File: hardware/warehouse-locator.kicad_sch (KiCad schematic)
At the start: 12 parts, among them J1 Screw_Terminal_01x03, J2 Screw_Terminal_01x03, J3 Screw_Terminal_01x03, J4 Barrel_Jack, J5 Screw_Terminal_01x03, J6 Screw_Terminal_01x03, J7 Screw_Terminal_01x03, J8 Ethernet, U1 ESP32-DevKitC

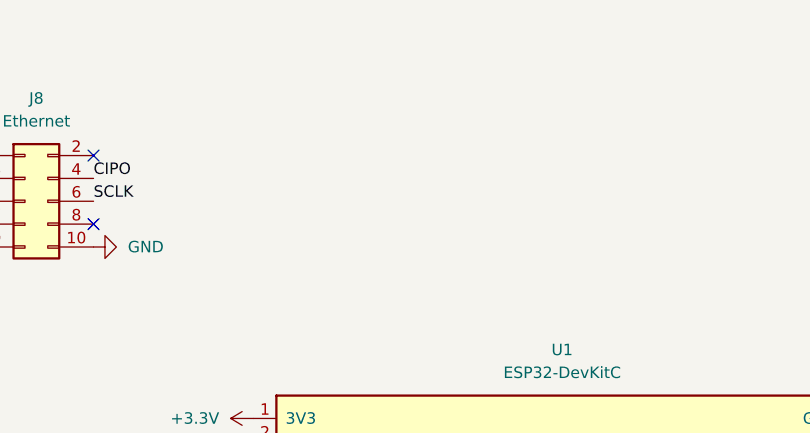
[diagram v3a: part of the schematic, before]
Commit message: Add Status LED
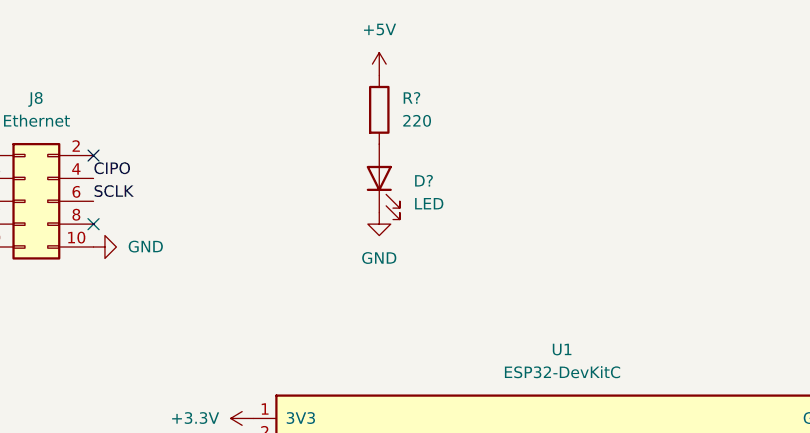
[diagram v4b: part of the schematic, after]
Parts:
- added D?: LED, LED_THT:LED_D5.0mm, symbol Device:LED
- added R?: 220, Resistor_THT:R_Axial_DIN0207_L6.3mm_D2.5mm_P10.16mm_Horizontal, symbol Device:R
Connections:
- net +5V: now also R?.1
- net GND: now also D?.1 (K)
- new net: D?.2 (A), R?.2
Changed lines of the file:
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@@
     (pin "3")
+  )
+  (symbol (lib_id "Device:LED") (at 179.07 54.61 90) (unit 1)
+    (in_bom yes) (on_board yes) (fields_autoplaced)
+    (property "Reference" "D?" (id 0) (at 182.88 54.9274 90)
+      (effects (font (size 1.27 1.27)) (justify right))
+    )
+    (property "Value" "LED" (id 1) (at 182.88 57.4674 90)
+      (effects (font (size 1.27 1.27)) (justify right))
+    )
+    (property "Footprint" "LED_THT:LED_D5.0mm" (id 2) (at 179.07 54.61 0)
+      (effects (font (size 1.27 1.27)) hide)
+    )
+    (property "Datasheet" "~" (id 3) (at 179.07 54.61 0)
+      (effects (font (size 1.27 1.27)) hide)
+    )
+    (pin "1")
+    (pin "2")
   )
   (symbol (lib_name "GND_1") (lib_id "power:GND") (at 238.76 81.28 90) (unit 1)
@@
       (effects (font (size 1.27 1.27)) hide)
     )
+  )
+  (symbol (lib_name "GND_3") (lib_id "power:GND") (at 179.07 58.42 0) (unit 1)
+    (in_bom yes) (on_board yes) (fields_autoplaced)
+    (property "Reference" "#PWR?" (id 0) (at 179.07 64.77 0)
+      (effects (font (size 1.27 1.27)) hide)
+    )
+    (property "Value" "GND" (id 1) (at 179.07 63.5 0))
+    (property "Footprint" "" (id 2) (at 179.07 58.42 0)
+      (effects (font (size 1.27 1.27)) hide)
+    )
+    (property "Datasheet" "" (id 3) (at 179.07 58.42 0)
+      (effects (font (size 1.27 1.27)) hide)
+    )
+    (pin "1")
   )
   (symbol (lib_id "power:+5V") (at 59.69 101.6 0) (unit 1)
@@
     (pin "1")
   )
+  (symbol (lib_name "+5V_1") (lib_id "power:+5V") (at 179.07 43.18 0) (unit 1)
+    (in_bom yes) (on_board yes) (fields_autoplaced)
+    (property "Reference" "#PWR?" (id 0) (at 179.07 46.99 0)
+      (effects (font (size 1.27 1.27)) hide)
+    )
+    (property "Value" "+5V" (id 1) (at 179.07 38.1 0))
+    (property "Footprint" "" (id 2) (at 179.07 43.18 0)
+      (effects (font (size 1.27 1.27)) hide)
+    )
+    (property "Datasheet" "" (id 3) (at 179.07 43.18 0)
+      (effects (font (size 1.27 1.27)) hide)
+    )
+    (pin "1")
+  )
   (symbol (lib_id "Connector:Screw_Terminal_01x03") (at 102.87 105.41 0) (unit 1)
     (in_bom yes) (on_board yes) (fields_autoplaced)
@@
     (pin "2")
     (pin "3")
+  )
+  (symbol (lib_id "Device:R") (at 179.07 46.99 0) (unit 1)
+    (in_bom yes) (on_board yes) (fields_autoplaced)
+    (property "Reference" "R?" (id 0) (at 181.61 45.7199 0)
+      (effects (font (size 1.27 1.27)) (justify left))
+    )
+    (property "Value" "220" (id 1) (at 181.61 48.2599 0)
+      (effects (font (size 1.27 1.27)) (justify left))
+    )
+    (property "Footprint" "Resistor_THT:R_Axial_DIN0207_L6.3mm_D2.5mm_P10.16mm_Horizontal" (id 2) (at 177.292 46.99 90)
+      (effects (font (size 1.27 1.27)) hide)
+    )
+    (property "Datasheet" "~" (id 3) (at 179.07 46.99 0)
+      (effects (font (size 1.27 1.27)) hide)
+    )
+    (pin "1")
+    (pin "2")
   )
   (symbol (lib_id "power:GND") (at 59.69 130.81 0) (unit 1)
@@
       (reference "#PWR?") (unit 1) (value "GND") (footprint "")
     )
+    (path "/49326297-d7a8-49d2-98aa-68a298420de1"
+      (reference "#PWR?") (unit 1) (value "GND") (footprint "")
+    )
     (path "/b6dc58df-5635-4bfb-a0b6-f31ca3e9691d"
       (reference "#PWR?") (unit 1) (value "GND") (footprint "")
@@
       (reference "#PWR?") (unit 1) (value "+3.3V") (footprint "")
     )
+    (path "/bbb94cab-5b50-47f4-b8eb-61d575e804ee"
+      (reference "#PWR?") (unit 1) (value "+5V") (footprint "")
+    )
+    (path "/1db8de92-1b7e-4ee2-8b02-085abde4cb76"
+      (reference "D?") (unit 1) (value "LED") (footprint "LED_THT:LED_D5.0mm")
+    )
     (path "/3f6f5fd4-bf84-4f5a-b527-b698f4821ee8"
       (reference "H1") (unit 1) (value "MountingHole") (footprint "MountingHole:MountingHole_3.2mm_M3_DIN965_Pad")
@@
       (reference "J8") (unit 1) (value "Ethernet") (footprint "Connector_PinSocket_2.54mm:PinSocket_2x05_P2.54mm_Vertical")
     )
+    (path "/cb16680a-c0f0-4315-a6bd-4d57dd5f9f7f"
+      (reference "R?") (unit 1) (value "220") (footprint "Resistor_THT:R_Axial_DIN0207_L6.3mm_D2.5mm_P10.16mm_Horizontal")
+    )
     (path "/8a6d48a6-b7bb-4a02-b51b-9f669ac7dca2"

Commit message: Commit missing file
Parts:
- gave numbers to parts that had none: 2
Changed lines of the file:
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@@
   (symbol (lib_id "power:+5V") (at 165.1 127 90) (unit 1)
     (in_bom yes) (on_board yes)
-    (property "Reference" "#PWR?" (id 0) (at 168.91 127 0)
+    (property "Reference" "#PWR019" (id 0) (at 168.91 127 0)
       (effects (font (size 1.27 1.27)) hide)
     )
@@
   (symbol (lib_name "GND_2") (lib_id "power:GND") (at 165.1 114.3 270) (unit 1)
     (in_bom yes) (on_board yes) (fields_autoplaced)
-    (property "Reference" "#PWR?" (id 0) (at 158.75 114.3 0)
+    (property "Reference" "#PWR018" (id 0) (at 158.75 114.3 0)
       (effects (font (size 1.27 1.27)) hide)
     )
@@
   (symbol (lib_id "Device:LED") (at 179.07 54.61 90) (unit 1)
     (in_bom yes) (on_board yes) (fields_autoplaced)
-    (property "Reference" "D?" (id 0) (at 182.88 54.9274 90)
+    (property "Reference" "D1" (id 0) (at 182.88 54.9274 90)
       (effects (font (size 1.27 1.27)) (justify right))
     )
@@
   (symbol (lib_name "GND_1") (lib_id "power:GND") (at 238.76 81.28 90) (unit 1)
     (in_bom yes) (on_board yes) (fields_autoplaced)
-    (property "Reference" "#PWR?" (id 0) (at 245.11 81.28 0)
+    (property "Reference" "#PWR022" (id 0) (at 245.11 81.28 0)
       (effects (font (size 1.27 1.27)) hide)
     )
@@
   (symbol (lib_name "GND_3") (lib_id "power:GND") (at 179.07 58.42 0) (unit 1)
     (in_bom yes) (on_board yes) (fields_autoplaced)
-    (property "Reference" "#PWR?" (id 0) (at 179.07 64.77 0)
+    (property "Reference" "#PWR021" (id 0) (at 179.07 64.77 0)
       (effects (font (size 1.27 1.27)) hide)
     )
@@
   (symbol (lib_name "GND_1") (lib_id "power:GND") (at 238.76 96.52 90) (unit 1)
     (in_bom yes) (on_board yes) (fields_autoplaced)
-    (property "Reference" "#PWR?" (id 0) (at 245.11 96.52 0)
+    (property "Reference" "#PWR023" (id 0) (at 245.11 96.52 0)
       (effects (font (size 1.27 1.27)) hide)
     )
@@
   (symbol (lib_id "power:+3.3V") (at 165.1 81.28 90) (unit 1)
     (in_bom yes) (on_board yes) (fields_autoplaced)
-    (property "Reference" "#PWR?" (id 0) (at 168.91 81.28 0)
+    (property "Reference" "#PWR017" (id 0) (at 168.91 81.28 0)
       (effects (font (size 1.27 1.27)) hide)
     )
@@
   (symbol (lib_name "+5V_1") (lib_id "power:+5V") (at 179.07 43.18 0) (unit 1)
     (in_bom yes) (on_board yes) (fields_autoplaced)
-    (property "Reference" "#PWR?" (id 0) (at 179.07 46.99 0)
+    (property "Reference" "#PWR020" (id 0) (at 179.07 46.99 0)
       (effects (font (size 1.27 1.27)) hide)
     )
@@
   (symbol (lib_id "Device:R") (at 179.07 46.99 0) (unit 1)
     (in_bom yes) (on_board yes) (fields_autoplaced)
-    (property "Reference" "R?" (id 0) (at 181.61 45.7199 0)
+    (property "Reference" "R1" (id 0) (at 181.61 45.7199 0)
       (effects (font (size 1.27 1.27)) (justify left))
     )
@@
       (reference "#PWR016") (unit 1) (value "GND") (footprint "")
     )
+    (path "/b8c97f6d-2826-4abe-9a0d-fbf24acc9464"
+      (reference "#PWR017") (unit 1) (value "+3.3V") (footprint "")
+    )
+    (path "/0ff64a17-acbe-42e6-b6e4-0d8dd8c401b1"
+      (reference "#PWR018") (unit 1) (value "GND") (footprint "")
+    )
     (path "/0254aefe-66fc-4322-8d36-d41b0cd7ed4c"
-      (reference "#PWR?") (unit 1) (value "+5V") (footprint "")
-    )
-    (path "/0ff64a17-acbe-42e6-b6e4-0d8dd8c401b1"
-      (reference "#PWR?") (unit 1) (value "GND") (footprint "")
+      (reference "#PWR019") (unit 1) (value "+5V") (footprint "")
+    )
+    (path "/bbb94cab-5b50-47f4-b8eb-61d575e804ee"
+      (reference "#PWR020") (unit 1) (value "+5V") (footprint "")
+    )
+    (path "/49326297-d7a8-49d2-98aa-68a298420de1"
+      (reference "#PWR021") (unit 1) (value "GND") (footprint "")
     )
     (path "/213ea978-248f-4385-b520-aff4ee3ab8b6"
-      (reference "#PWR?") (unit 1) (value "GND") (footprint "")
-    )
-    (path "/49326297-d7a8-49d2-98aa-68a298420de1"
-      (reference "#PWR?") (unit 1) (value "GND") (footprint "")
+      (reference "#PWR022") (unit 1) (value "GND") (footprint "")
     )
     (path "/b6dc58df-5635-4bfb-a0b6-f31ca3e9691d"
-      (reference "#PWR?") (unit 1) (value "GND") (footprint "")
-    )
-    (path "/b8c97f6d-2826-4abe-9a0d-fbf24acc9464"
-      (reference "#PWR?") (unit 1) (value "+3.3V") (footprint "")
-    )
-    (path "/bbb94cab-5b50-47f4-b8eb-61d575e804ee"
-      (reference "#PWR?") (unit 1) (value "+5V") (footprint "")
+      (reference "#PWR023") (unit 1) (value "GND") (footprint "")
     )
     (path "/1db8de92-1b7e-4ee2-8b02-085abde4cb76"
-      (reference "D?") (unit 1) (value "LED") (footprint "LED_THT:LED_D5.0mm")
+      (reference "D1") (unit 1) (value "LED") (footprint "LED_THT:LED_D5.0mm")
     )
     (path "/3f6f5fd4-bf84-4f5a-b527-b698f4821ee8"
@@
     )
     (path "/cb16680a-c0f0-4315-a6bd-4d57dd5f9f7f"
-      (reference "R?") (unit 1) (value "220") (footprint "Resistor_THT:R_Axial_DIN0207_L6.3mm_D2.5mm_P10.16mm_Horizontal")
+      (reference "R1") (unit 1) (value "220") (footprint "Resistor_THT:R_Axial_DIN0207_L6.3mm_D2.5mm_P10.16mm_Horizontal")
     )
     (path "/8a6d48a6-b7bb-4a02-b51b-9f669ac7dca2"
